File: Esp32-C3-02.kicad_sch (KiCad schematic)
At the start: 30 parts, among them J3 GSD090012SEU, U2 USBLC6-2SC6, U3 ESP32-C3-WROOM-02, U4 CP2102N-Axx-xQFN20, U5 W25Q16JVSS

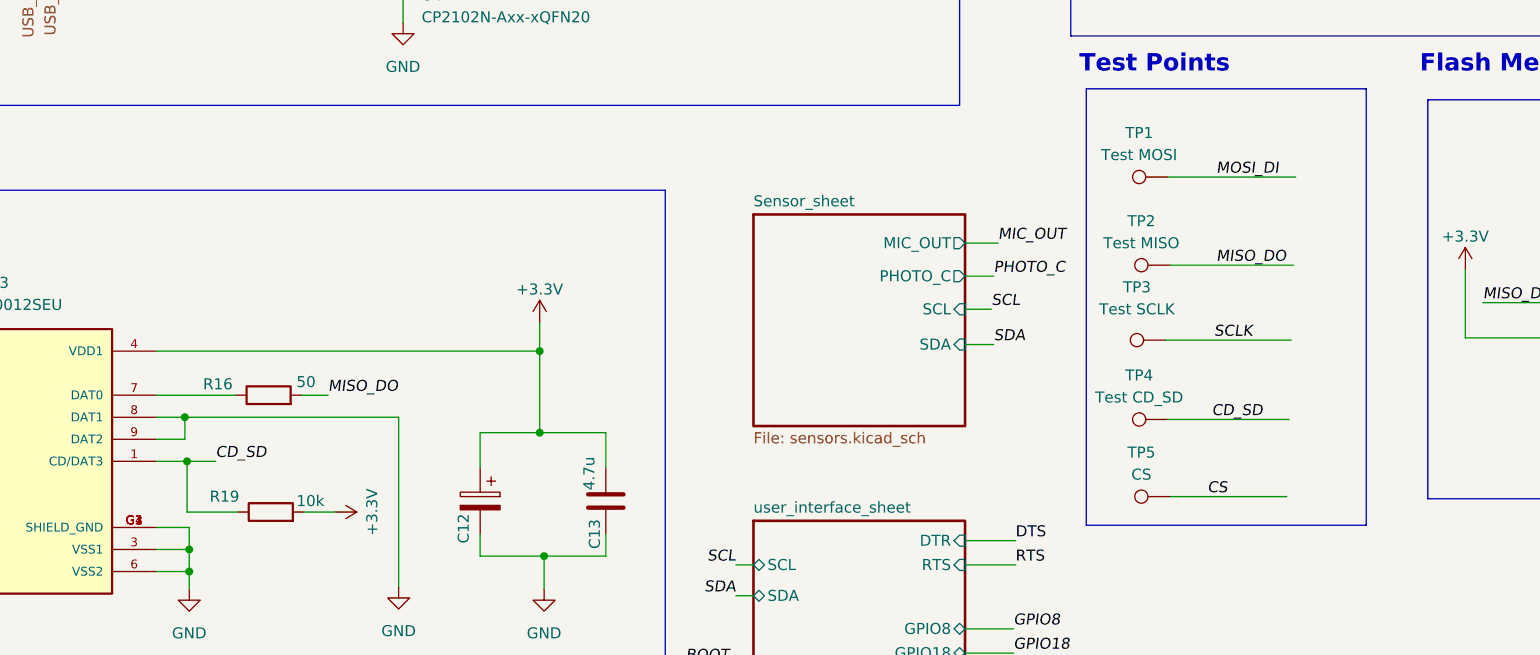
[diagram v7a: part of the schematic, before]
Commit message: run ERC check for the schematic
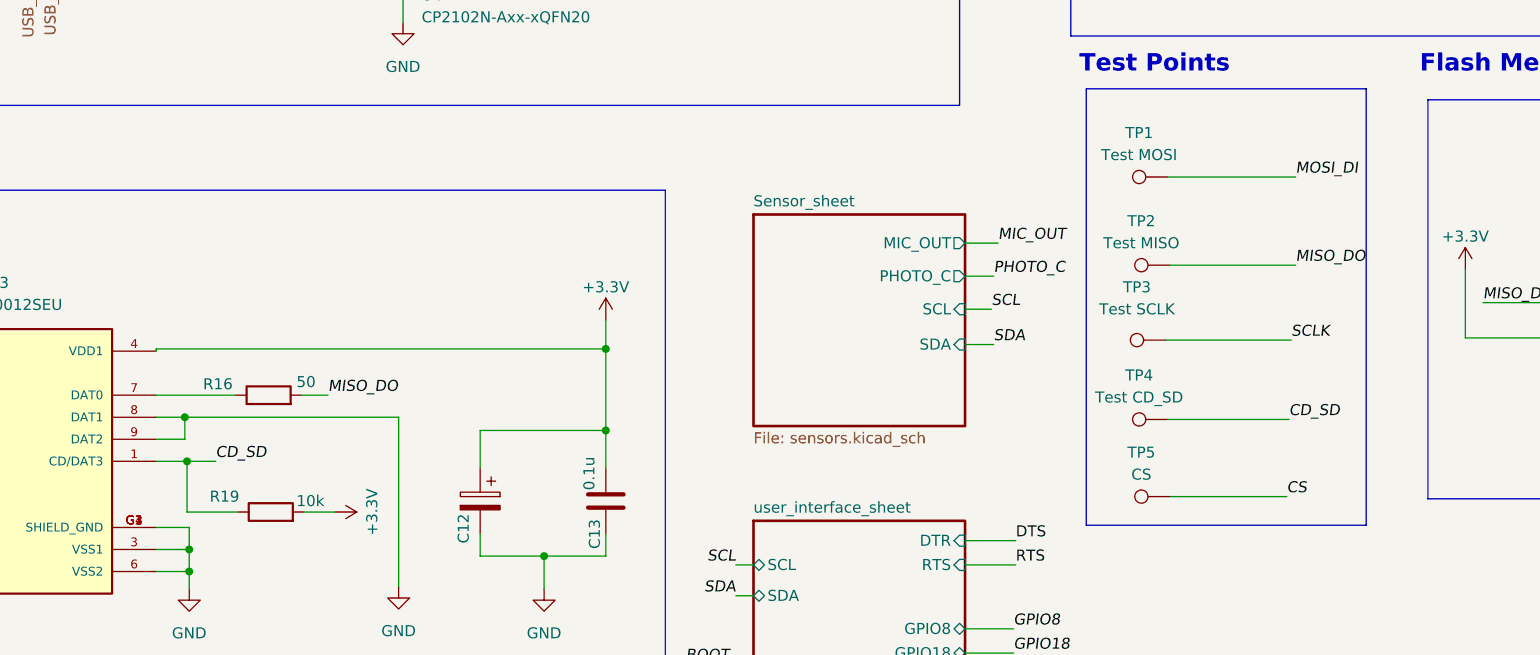
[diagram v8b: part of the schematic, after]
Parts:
- C10, C11, C14, C8: footprint (none) -> Capacitor_SMD:C_0805_2012Metric
- C12, C7, C9: footprint (none) -> Capacitor_Tantalum_SMD:CP_EIA-7343-40_Kemet-Y
- C13: value 4.7u -> 0.1u; footprint (none) -> Capacitor_SMD:C_0805_2012Metric
- LED5, LED6: footprint LED_LTST-C170KGKT_LTO -> LED_SMD:LED_0805_2012Metric
- R11, R12, R13, R14, R15, R16, R18, R19, R20, R22: footprint (none) -> Resistor_SMD:R_0805_2012Metric
- TP1, TP2, TP3, TP4, TP5: footprint (none) -> TestPoint:TestPoint_Pad_D1.0mm
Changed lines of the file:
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@@
 	)
 	(junction
-		(at 108.204 143.256)
+		(at 115.824 143.002)
 		(diameter 0)
 		(color 0 0 0 0)
@@
 	)
 	(junction
-		(at 108.204 152.654)
+		(at 115.824 152.4)
 		(diameter 0)
 		(color 0 0 0 0)
@@
 	(wire
 		(pts
-			(xy 108.204 152.654) (xy 101.346 152.654)
+			(xy 115.824 152.4) (xy 101.346 152.4)
 		)
 		(stroke
@@
 	(wire
 		(pts
-			(xy 108.204 143.256) (xy 108.204 152.654)
+			(xy 115.824 143.002) (xy 115.824 152.4)
 		)
 		(stroke
@@
 	(wire
 		(pts
-			(xy 115.824 152.654) (xy 108.204 152.654)
+			(xy 116.078 152.4) (xy 115.824 152.4)
 		)
 		(stroke
@@
 	(wire
 		(pts
-			(xy 64.008 143.256) (xy 108.204 143.256)
+			(xy 64.008 143.002) (xy 115.824 143.002)
+		)
+		(stroke
+			(width 0)
+			(type default)
+		)
+	)
+	(wire
+		(pts
+			(xy 64.008 143.002) (xy 64.008 143.256)
 		)
 		(stroke
@@
 	(wire
 		(pts
-			(xy 101.346 152.654) (xy 101.346 156.718)
+			(xy 101.346 152.4) (xy 101.346 156.718)
 		)
 		(stroke
@@
 	(wire
 		(pts
-			(xy 115.824 152.654) (xy 115.824 156.718)
+			(xy 116.078 152.4) (xy 116.078 152.654)
 		)
 		(stroke
@@
 	(wire
 		(pts
+			(xy 116.078 152.654) (xy 115.824 152.654)
+		)
+		(stroke
+			(width 0)
+			(type default)
+		)
+	)
+	(wire
+		(pts
 			(xy 157.226 130.81) (xy 161.036 130.81)
 		)
@@
 	(wire
 		(pts
-			(xy 180.848 133.35) (xy 195.072 133.35)
+			(xy 180.848 133.35) (xy 195.326 133.35)
 		)
 		(stroke
@@
 	(wire
 		(pts
+			(xy 115.824 152.654) (xy 115.824 156.718)
+		)
+		(stroke
+			(width 0)
+			(type default)
+		)
+	)
+	(wire
+		(pts
 			(xy 108.331 92.71) (xy 108.331 89.535)
 		)
@@
 	(wire
 		(pts
-			(xy 108.204 139.954) (xy 108.204 143.256)
+			(xy 115.824 139.7) (xy 115.824 143.002)
 		)
 		(stroke
@@
 	)
 	(label "CD_SD"
-		(at 185.674 151.13 0)
+		(at 194.564 151.13 0)
 		(effects
 			(font
@@
 	)
 	(label "CS"
-		(at 185.166 160.02 0)
+		(at 194.31 160.02 0)
 		(effects
 			(font
@@
 	)
 	(label "MOSI_DI"
-		(at 186.182 123.19 0)
+		(at 195.326 123.19 0)
 		(effects
 			(font
@@
 	)
 	(label "SCLK"
-		(at 185.928 141.986 0)
+		(at 194.818 141.986 0)
 		(effects
 			(font
@@
 	)
 	(label "MISO_DO"
-		(at 186.182 133.35 0)
+		(at 195.326 133.35 0)
 		(effects
 			(font
@@
 			)
 		)
-		(property "Footprint" ""
+		(property "Footprint" "Resistor_SMD:R_0805_2012Metric"
 			(at 119.126 85.598 90)
 			(effects
@@
 			)
 		)
-		(property "Footprint" ""
+		(property "Footprint" "Capacitor_Tantalum_SMD:CP_EIA-7343-40_Kemet-Y"
 			(at 63.881 29.5148 0)
 			(effects
@@
 			)
 		)
-		(property "Footprint" ""
+		(property "Footprint" "Resistor_SMD:R_0805_2012Metric"
 			(at 76.962 150.114 90)
 			(effects
@@
 			)
 		)
-		(property "Footprint" ""
+		(property "Footprint" "Resistor_SMD:R_0805_2012Metric"
 			(at 191.262 73.406 90)
 			(effects
@@
 			)
 		)
-		(property "Footprint" ""
+		(property "Footprint" "Resistor_SMD:R_0805_2012Metric"
 			(at 233.426 139.446 90)
 			(effects
@@
 			)
 		)
-		(property "Value" "4.7u"
+		(property "Value" "0.1u"
 			(at 113.919 157.353 90)
 			(effects
@@
 			)
 		)
-		(property "Footprint" ""
+		(property "Footprint" "Capacitor_SMD:C_0805_2012Metric"
 			(at 114.8588 164.338 0)
 			(effects
@@
 			)
 		)
-		(property "Footprint" ""
+		(property "Footprint" "Capacitor_SMD:C_0805_2012Metric"
 			(at 269.1892 137.922 0)
 			(effects
@@
 			)
 		)
-		(property "Footprint" ""
+		(property "Footprint" "TestPoint:TestPoint_Pad_D1.0mm"
 			(at 180.594 146.05 0)
 			(effects
@@
 	(symbol
 		(lib_id "power:+3.3V")
-		(at 108.204 139.954 0)
+		(at 115.824 139.7 0)
 		(unit 1)
 		(exclude_from_sim no)
@@
 		(dnp no)
 		(property "Reference" "#PWR036"
-			(at 108.204 143.764 0)
+			(at 115.824 143.51 0)
 			(effects
 				(font
@@
 		)
 		(property "Value" "+3.3V"
-			(at 108.204 136.144 0)
+			(at 115.824 135.89 0)
 			(effects
 				(font
@@
 		)
 		(property "Footprint" ""
-			(at 108.204 139.954 0)
+			(at 115.824 139.7 0)
 			(effects
 				(font
@@
 		)
 		(property "Datasheet" ""
-			(at 108.204 139.954 0)
+			(at 115.824 139.7 0)
 			(effects
 				(font
@@
 		)
 		(property "Description" "Power symbol creates a global label with name \"+3.3V\""
-			(at 108.204 139.954 0)
+			(at 115.824 139.7 0)
 			(effects
 				(font
@@
 			)
 		)
-		(property "Footprint" ""
+		(property "Footprint" "Resistor_SMD:R_0805_2012Metric"
 			(at 77.216 163.576 90)
 			(effects
@@
 			)
 		)
-		(property "Footprint" "LED_LTST-C170KGKT_LTO"
+		(property "Footprint" "LED_SMD:LED_0805_2012Metric"
 			(at 138.176 92.71 0)
 			(effects
@@
 			)
 		)
-		(property "Footprint" ""
+		(property "Footprint" "Capacitor_SMD:C_0805_2012Metric"
 			(at 63.881 37.1348 0)
 			(effects
@@
 			)
 		)
-		(property "Footprint" ""
+		(property "Footprint" "Resistor_SMD:R_0805_2012Metric"
 			(at 18.923 55.245 90)
 			(effects
@@
 			)
 		)
-		(property "Footprint" ""
+		(property "Footprint" "TestPoint:TestPoint_Pad_D1.0mm"
 			(at 180.848 128.27 0)
 			(effects
@@
 			)
 		)
-		(property "Footprint" "LED_LTST-C170KGKT_LTO"
+		(property "Footprint" "LED_SMD:LED_0805_2012Metric"
 			(at 138.176 83.82 0)
 			(effects
@@
 			)
 		)
-		(property "Footprint" ""
+		(property "Footprint" "Capacitor_Tantalum_SMD:CP_EIA-7343-40_Kemet-Y"
 			(at 263.8552 72.39 0)
 			(effects
@@
 			)
 		)
-		(property "Footprint" ""
+		(property "Footprint" "Resistor_SMD:R_0805_2012Metric"
 			(at 18.923 71.755 90)
 			(effects
@@
 			)
 		)
-		(property "Footprint" ""
+		(property "Footprint" "Capacitor_SMD:C_0805_2012Metric"
 			(at 248.1072 72.39 0)
 			(effects
@@
 			)
 		)
-		(property "Footprint" ""
+		(property "Footprint" "TestPoint:TestPoint_Pad_D1.0mm"
 			(at 180.34 136.906 0)
 			(effects
@@
 			)
 		)
-		(property "Footprint" ""
+		(property "Footprint" "TestPoint:TestPoint_Pad_D1.0mm"
 			(at 180.848 154.94 0)
 			(effects
@@
 			)
 		)
-		(property "Footprint" ""
+		(property "Footprint" "TestPoint:TestPoint_Pad_D1.0mm"
 			(at 180.594 118.11 0)
 			(effects
@@
 			)
 		)
-		(property "Footprint" ""
+		(property "Footprint" "Resistor_SMD:R_0805_2012Metric"
 			(at 191.008 81.534 90)
 			(effects
@@
 			)
 		)
-		(property "Footprint" ""
+		(property "Footprint" "Capacitor_Tantalum_SMD:CP_EIA-7343-40_Kemet-Y"
 			(at 100.3808 164.338 0)
 			(effects
@@
 			)
 		)
-		(property "Footprint" ""
+		(property "Footprint" "Capacitor_SMD:C_0805_2012Metric"
 			(at 36.2712 76.2 0)
 			(effects
@@
 			)
 		)
-		(property "Footprint" ""
+		(property "Footprint" "Resistor_SMD:R_0805_2012Metric"
 			(at 119.126 94.488 90)
 			(effects
@@
 			)
 		)
-		(property "Footprint" ""
+		(property "Footprint" "Resistor_SMD:R_0805_2012Metric"
 			(at 63.246 53.213 90)
 			(effects
